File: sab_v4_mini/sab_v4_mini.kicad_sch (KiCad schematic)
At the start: 0 parts

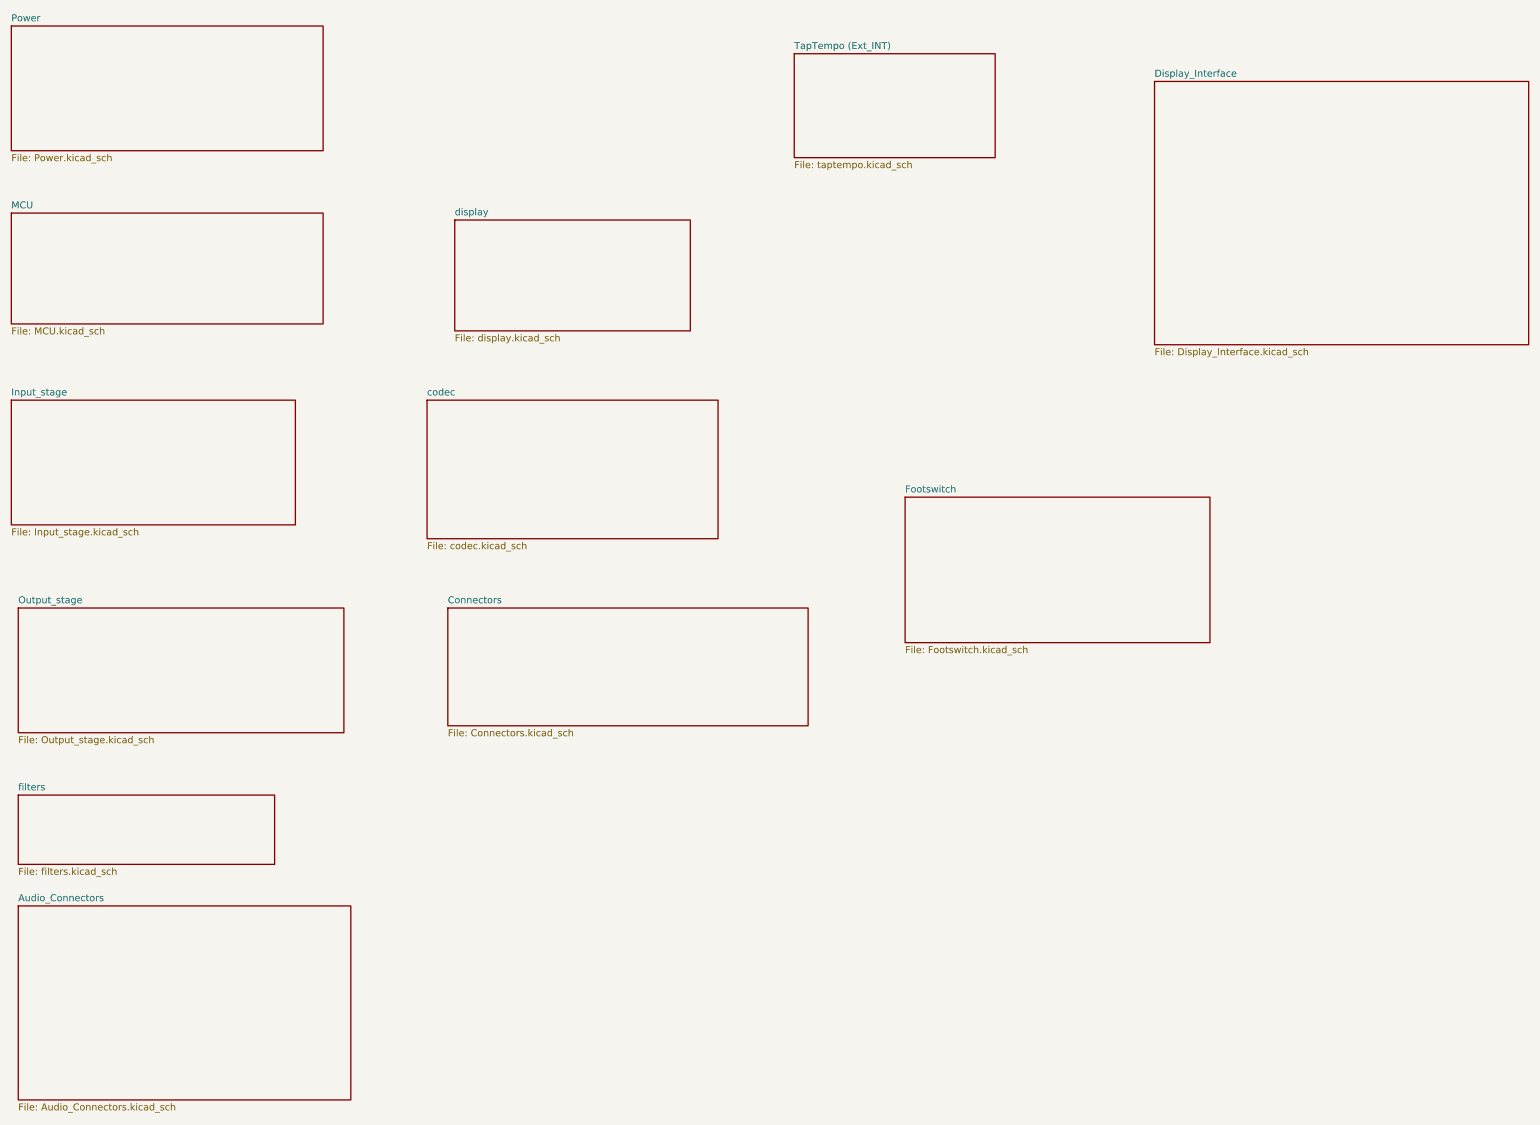
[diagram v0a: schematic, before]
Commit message: Delete unused pages
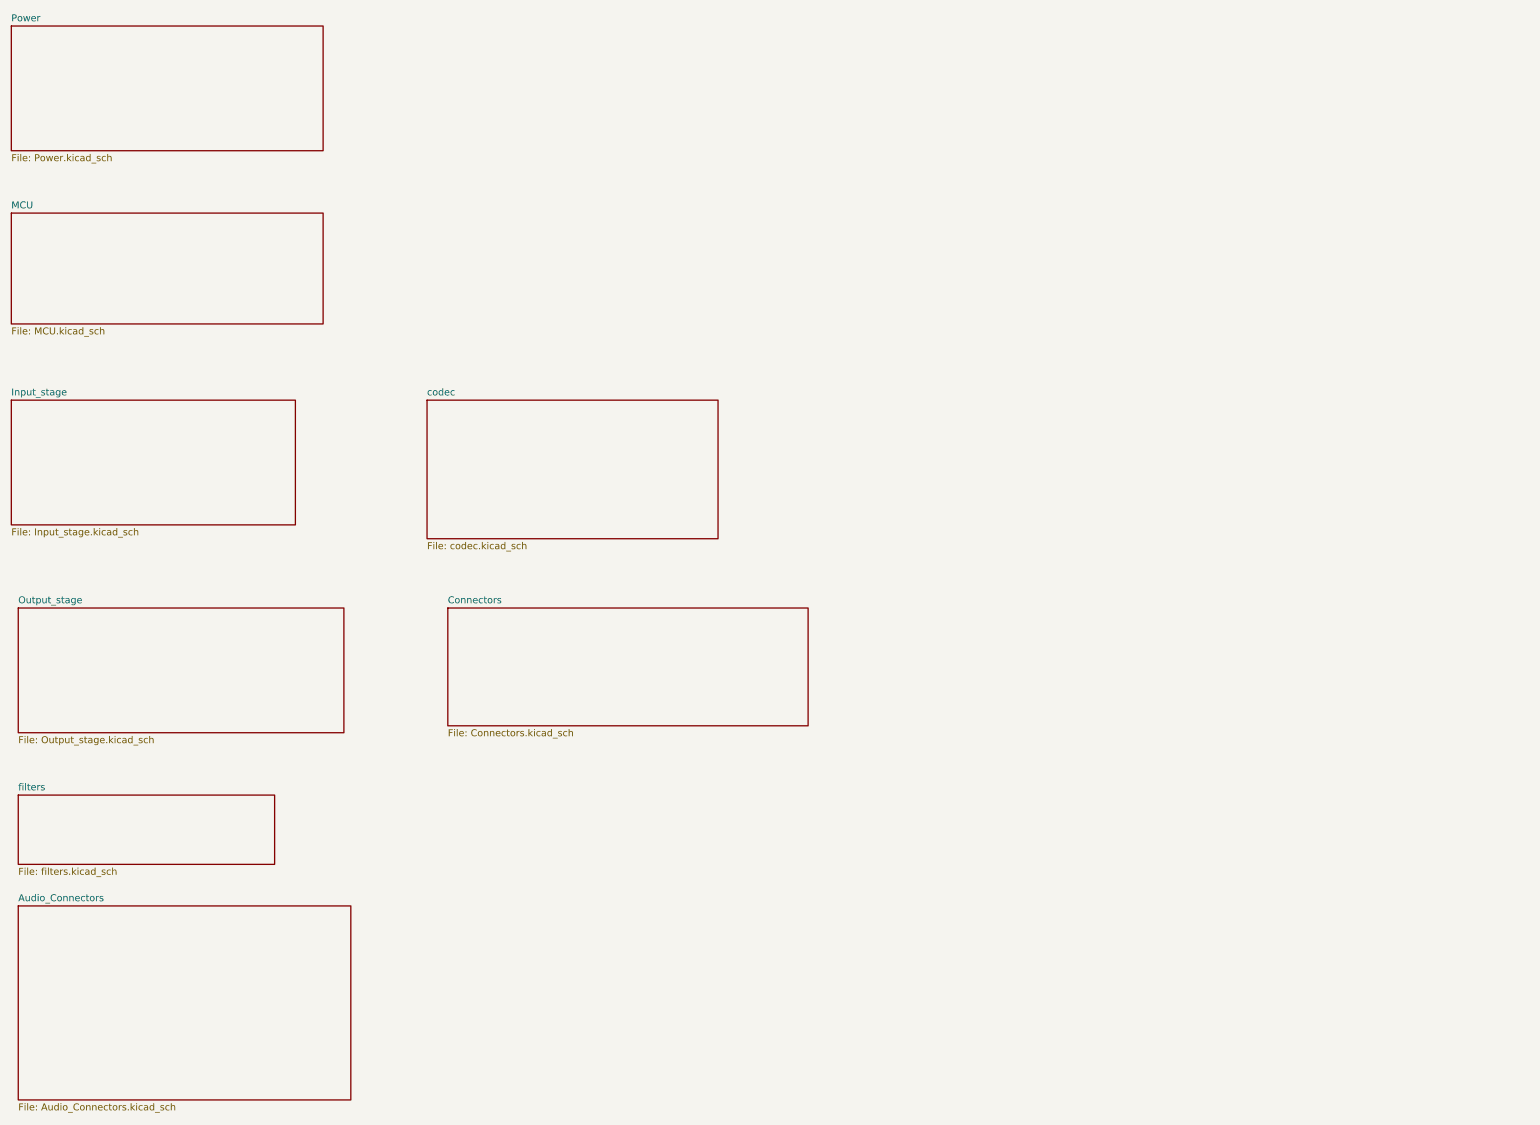
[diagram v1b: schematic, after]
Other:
- removed sheet Display_Interface
- removed sheet Footswitch
- removed sheet TapTempo (Ext_INT)
- removed sheet display
